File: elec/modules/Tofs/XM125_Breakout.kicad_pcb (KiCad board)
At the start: 2 copper layers, 25.4 x 50.8 mm, 97 parts, among them J13 SWD (DNP), J2 RIGHT_ANGLE, J3 RIGHT_ANGLE, U1 XM125, U2 RT9080-33GJ5, U3 RT9080-18GJ5, U4 CH340C, U5 ESD Diode

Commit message: made schematics more organised ish for tofs
Hope i didnt mess anyuthingn  up
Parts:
- removed FRAME2: FRAME-LETTER, CREATIVE_COMMONS
- removed LOGO5: SFE_LOGO_FLAME.1_INCH, SFE_LOGO_FLAME_.1
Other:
- board text removed: "M. Chodikov"
- board text removed: "v10"

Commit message: tofs:debranded it and added 1 via to add gnd fill
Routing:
- net GND: vias 42 -> 43
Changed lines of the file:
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@@
+	)
+	(segment
+		(start 149.2631 95.2246)
+		(end 149.2631 93)
+		(width 0.508)
+		(layer "B.Cu")
+		(net 2)
 	)
 	(segment
@@
 	)
 	(segment
-		(start 149.2631 92.5576)
-		(end 149.1361 92.4306)
-		(width 0.508)
-		(layer "B.Cu")
-		(net 2)
-	)
-	(segment
 		(start 156.1211 121.3866)
 		(end 156.1211 119.4816)
@@
 	)
 	(segment
+		(start 149.1361 92.873)
+		(end 149.1361 91.4086)
+		(width 0.508)
+		(layer "B.Cu")
+		(net 2)
+	)
+	(segment
 		(start 145.9611 113.7666)
 		(end 145.0721 112.8776)
@@
 	)
 	(segment
-		(start 149.1361 92.4306)
-		(end 149.1361 91.4086)
-		(width 0.508)
-		(layer "B.Cu")
-		(net 2)
-	)
-	(segment
 		(start 148.1811 105.4456)
 		(end 147.9931 105.2576)
@@
 	)
 	(segment
+		(start 149.2631 93)
+		(end 149.1361 92.873)
+		(width 0.508)
+		(layer "B.Cu")
+		(net 2)
+	)
+	(segment
 		(start 149.8012 101.3816)
 		(end 150.7871 101.3816)
@@
 		(start 147.9931 104.2416)
 		(end 150.7871 104.2416)
-		(width 0.508)
-		(layer "B.Cu")
-		(net 2)
-	)
-	(segment
-		(start 149.2631 95.2246)
-		(end 149.2631 92.5576)
 		(width 0.508)
 		(layer "B.Cu")
@@
 		(net 3)
 	)
+	(via
+		(at 142.5 92.75)
+		(size 0.6)
+		(drill 0.3)
+		(layers "F.Cu" "B.Cu")
+		(free yes)
+		(net 3)
+	)

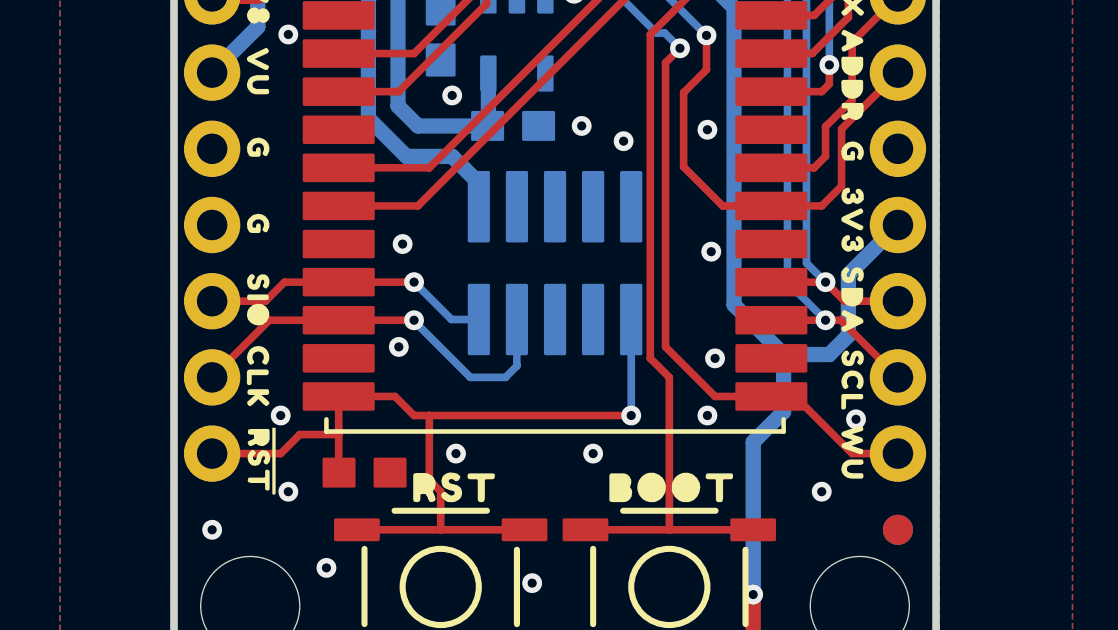
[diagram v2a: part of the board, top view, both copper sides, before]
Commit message: did pcba for tofs+increased dist between l1 to3 connection and sol activationi
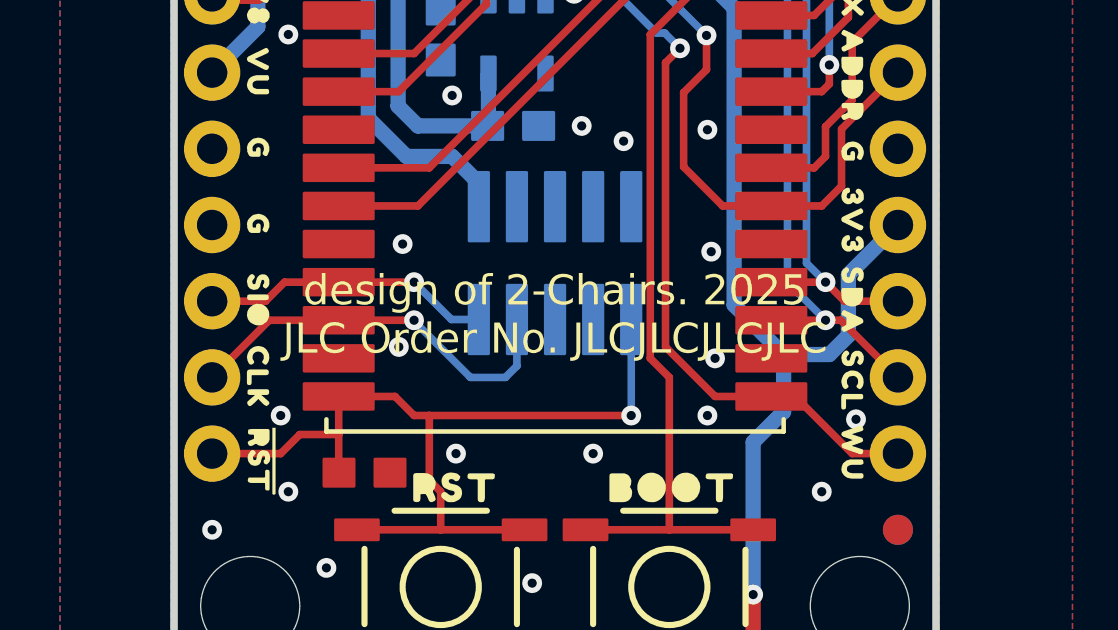
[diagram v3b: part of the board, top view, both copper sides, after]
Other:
- board text added: "design of 2-Chairs. 2025 JLC Order No. JLCJLCJLCJLC"
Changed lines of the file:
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@@
 			)
 		)
+		(attr exclude_from_pos_files exclude_from_bom)
 		(fp_poly
 			(pts
@@
 			)
 		)
+		(attr exclude_from_pos_files exclude_from_bom)
 		(fp_poly
 			(pts
@@
 			)
 		)
+		(attr exclude_from_pos_files exclude_from_bom)
 		(fp_poly
 			(pts
@@
 			)
 		)
+		(attr exclude_from_pos_files exclude_from_bom)
 		(fp_poly
 			(pts
@@
 			)
 		)
+		(attr exclude_from_pos_files exclude_from_bom)
 		(fp_circle
 			(center 0 0)
@@
 			)
 		)
+		(attr exclude_from_pos_files exclude_from_bom)
 		(pad "1" smd roundrect
 			(at 0 0)
@@
 			)
 		)
+		(attr exclude_from_pos_files exclude_from_bom)
 		(fp_poly
 			(pts
@@
 			)
 		)
+		(attr exclude_from_pos_files exclude_from_bom)
 		(fp_poly
 			(pts
@@
 			)
 		)
+		(attr exclude_from_pos_files exclude_from_bom)
 		(fp_poly
 			(pts
@@
 			)
 		)
+		(attr exclude_from_pos_files exclude_from_bom)
 		(fp_poly
 			(pts
@@
 			)
 		)
+		(attr exclude_from_pos_files exclude_from_bom)
 		(fp_poly
 			(pts
@@
 			)
 		)
+		(attr exclude_from_pos_files exclude_from_bom)
 		(fp_poly
 			(pts
@@
 			)
 		)
+		(attr exclude_from_pos_files exclude_from_bom)
 		(fp_poly
 			(pts
@@
 			)
 		)
+		(attr exclude_from_pos_files exclude_from_bom)
 		(fp_poly
 			(pts
@@
 			)
 		)
+		(attr exclude_from_pos_files exclude_from_bom)
 		(fp_poly
 			(pts
@@
 			)
 		)
+		(attr exclude_from_pos_files exclude_from_bom)
 		(fp_poly
 			(pts
@@
 			)
 		)
+		(attr exclude_from_pos_files exclude_from_bom)
 		(fp_circle
 			(center 0 0)
@@
 			)
 		)
+		(attr exclude_from_pos_files exclude_from_bom)
 		(fp_poly
 			(pts
@@
 			)
 		)
+		(attr exclude_from_pos_files exclude_from_bom)
 		(fp_line
 			(start -1.524 0.762)
@@
 			)
 		)
+		(attr exclude_from_pos_files exclude_from_bom)
 		(fp_poly
 			(pts
@@
 			)
 		)
+		(attr exclude_from_pos_files exclude_from_bom)
 		(fp_poly
 			(pts
@@
 			)
 		)
+		(attr exclude_from_pos_files exclude_from_bom)
 		(fp_poly
 			(pts
@@
 			)
 		)
+		(attr exclude_from_pos_files exclude_from_bom)
 		(fp_poly
 			(pts
@@
 			)
 		)
+		(attr exclude_from_pos_files exclude_from_bom)
 		(fp_poly
 			(pts
@@
 			)
 		)
+		(attr exclude_from_pos_files exclude_from_bom)
 		(fp_poly
 			(pts
@@
 			)
 		)
+		(attr exclude_from_pos_files exclude_from_bom)
 		(fp_poly
 			(pts
@@
 			)
 		)
+		(attr exclude_from_pos_files exclude_from_bom)
 		(fp_poly
 			(pts
@@
 			)
 		)
+		(attr exclude_from_pos_files exclude_from_bom)
 		(pad "1" smd roundrect
 			(at 0 0)
@@
 			)
 		)
+		(attr exclude_from_pos_files exclude_from_bom)
 		(fp_poly
 			(pts
@@
 			)
 		)
+		(attr exclude_from_pos_files exclude_from_bom)
 		(fp_line
 			(start 0 0)
@@
 			)
 		)
+		(attr exclude_from_pos_files exclude_from_bom)
 		(fp_poly
 			(pts
@@
 			)
 		)
+		(attr exclude_from_pos_files exclude_from_bom)
 		(fp_poly
 			(pts
@@
 			)
 		)
+		(attr exclude_from_pos_files exclude_from_bom)
 		(fp_poly
 			(pts
@@
 			)
 		)
+		(attr exclude_from_pos_files exclude_from_bom)
 		(fp_poly
 			(pts
@@
 			)
 		)
+		(attr exclude_from_pos_files exclude_from_bom)
 		(fp_poly
 			(pts
@@
 			)
 		)
+		(attr exclude_from_pos_files exclude_from_bom)
 		(fp_poly
 			(pts
@@
 			)
 		)
+		(attr exclude_from_pos_files exclude_from_bom)
 		(fp_poly
 			(pts
@@
 			)
 		)
+		(attr exclude_from_pos_files exclude_from_bom)
 		(fp_poly
 			(pts
@@
 			)
 		)
+		(attr exclude_from_pos_files exclude_from_bom)
 		(fp_circle
 			(center 0 0)
@@
 			)
 		)
+		(attr exclude_from_pos_files exclude_from_bom)
 		(fp_poly
 			(pts
@@
 			)
 		)
+		(attr exclude_from_pos_files exclude_from_bom)
 		(fp_poly
 			(pts
@@
 			)
 		)
+		(attr exclude_from_pos_files exclude_from_bom)
 		(fp_poly
 			(pts
@@
 			)
 		)
+		(attr exclude_from_pos_files exclude_from_bom)
 		(fp_poly
 			(pts
@@
 			)
 		)
+		(attr exclude_from_pos_files exclude_from_bom)
 		(fp_poly
 			(pts
@@
 			)
 		)
+		(attr exclude_from_pos_files exclude_from_bom)
 		(fp_circle
 			(center 0 0)
@@
 		)
 		(property "Datasheet" ""
-			(at 0 0 270)
+			(at 0 0 90)
 			(layer "F.Fab")
 			(hide yes)
@@
 		)
 		(property "Description" ""
-			(at 0 0 270)
+			(at 0 0 90)
 			(layer "F.Fab")
 			(hide yes)
@@
 			)
 		)
+		(attr exclude_from_pos_files exclude_from_bom)
 		(fp_poly
 			(pts
@@
 			)
 		)
+		(attr exclude_from_pos_files exclude_from_bom)
 		(fp_poly
 			(pts
@@
 			)
 		)
+		(attr exclude_from_pos_files exclude_from_bom)
 		(pad "1" smd roundrect
 			(at 0 0 180)
@@
 			)
 		)
+		(attr exclude_from_pos_files exclude_from_bom)
 		(fp_poly
 			(pts
@@
 			)
 		)
+		(attr exclude_from_pos_files exclude_from_bom)
 		(fp_poly
 			(pts
@@
 			)
 		)
+		(attr exclude_from_pos_files exclude_from_bom)
 		(fp_poly
 			(pts
@@
 			)
 		)
+		(attr exclude_from_pos_files exclude_from_bom)
 		(fp_poly
 			(pts
@@
 			)
 		)
+		(attr exclude_from_pos_files exclude_from_bom)
 		(fp_poly
 			(pts
@@
 			)
 		)
+		(attr exclude_from_pos_files exclude_from_bom)
 		(fp_poly
 			(pts
@@
 			)
 		)
+		(attr exclude_from_pos_files exclude_from_bom)
 		(fp_poly
 			(pts
@@
 			)
 		)
+		(attr exclude_from_pos_files exclude_from_bom)
 		(fp_poly
 			(pts
@@
 			)
 		)
+		(attr exclude_from_pos_files exclude_from_bom)
 		(fp_poly
 			(pts
@@
 			)
 		)
+		(attr exclude_from_pos_files exclude_from_bom)
 		(pad "1" smd roundrect
 			(at 0 0 180)
@@
 			)
 		)
+		(attr exclude_from_pos_files exclude_from_bom)
 		(fp_poly
 			(pts
@@
 			)
 		)
+		(attr exclude_from_pos_files exclude_from_bom)
 		(fp_poly
 			(pts
@@
 			)
 		)
+		(attr exclude_from_pos_files exclude_from_bom)
 		(fp_poly
 			(pts
@@
 			)
 		)
+		(attr exclude_from_pos_files exclude_from_bom)
 		(fp_poly
 			(pts
@@
 			)
 		)
+		(attr exclude_from_pos_files exclude_from_bom)
 		(fp_poly
 			(pts
@@
 			)
 		)
+		(attr exclude_from_pos_files exclude_from_bom)
 		(fp_poly
 			(pts
@@
 			)
 		)
+		(attr exclude_from_pos_files exclude_from_bom)
 		(fp_poly
 			(pts
@@
 			)
 		)
+		(attr exclude_from_pos_files exclude_from_bom)
 		(fp_poly
 			(pts
@@
 			)
 		)
+		(attr exclude_from_pos_files exclude_from_bom)
 		(fp_poly
 			(pts
@@
 			)
 		)
+		(attr exclude_from_pos_files exclude_from_bom)
 		(fp_poly
 			(pts
@@
 			)
 		)
+		(attr exclude_from_pos_files exclude_from_bom)
 		(fp_line
 			(start -3.26 1.715)
@@
 			)
 		)
+		(attr exclude_from_pos_files exclude_from_bom)
 		(fp_poly
 			(pts
@@
 			)
 		)
+		(attr exclude_from_pos_files exclude_from_bom)
 		(fp_poly
 			(pts
@@
 		(layer "Edge.Cuts")
 	)
+	(gr_text "design of 2-Chairs. 2025\nJLC Order No. JLCJLCJLCJLC"
+		(at 148.5011 118.1486 -0)
+		(layer "F.SilkS")
+		(effects
+			(font
+				(size 1 1)
+				(thickness 0.2)
+			)
+		)
+	)
 	(gr_text "Solder Mask: Red\nThickness: 1.6mm\nTwo layer design\nFinish: HASL Lead-Free\nCopper Weight: 1oz\nMaterial: TG135-140"

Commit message: prod: prod
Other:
- board text removed: "design of 2-Chairs. 2025 JLC Order No. JLCJLCJLCJLC"
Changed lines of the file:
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@@
 		(layer "Edge.Cuts")
-	)
-	(gr_text "design of 2-Chairs. 2025\nJLC Order No. JLCJLCJLCJLC"
-		(at 148.5011 118.1486 -0)
-		(layer "F.SilkS")
-		(effects
-			(font
-				(size 1 1)
-				(thickness 0.2)
-			)
-		)
 	)
 	(gr_text "Solder Mask: Red\nThickness: 1.6mm\nTwo layer design\nFinish: HASL Lead-Free\nCopper Weight: 1oz\nMaterial: TG135-140"
